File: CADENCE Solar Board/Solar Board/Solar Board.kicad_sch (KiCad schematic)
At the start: 44 parts, among them J1 Conn_01x08, U1 INA230AIRGTT, U2 AD7414ARTZ-1REEL7, U3 OPT3001IDNPRQ1

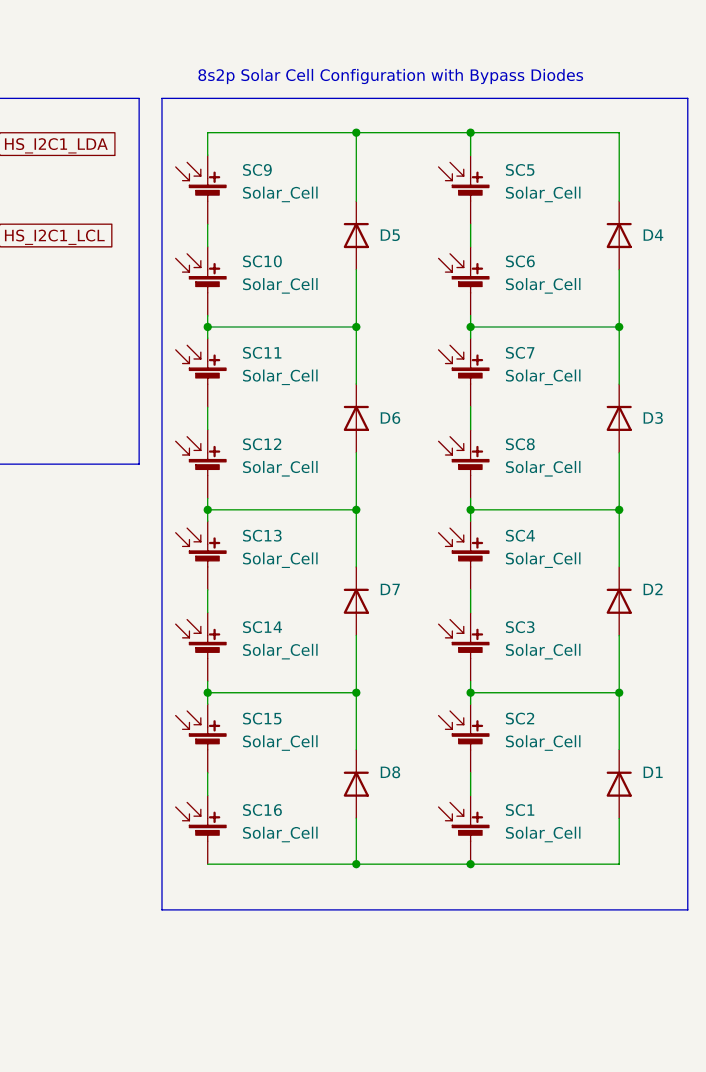
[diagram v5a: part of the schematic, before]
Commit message: fixed diodes
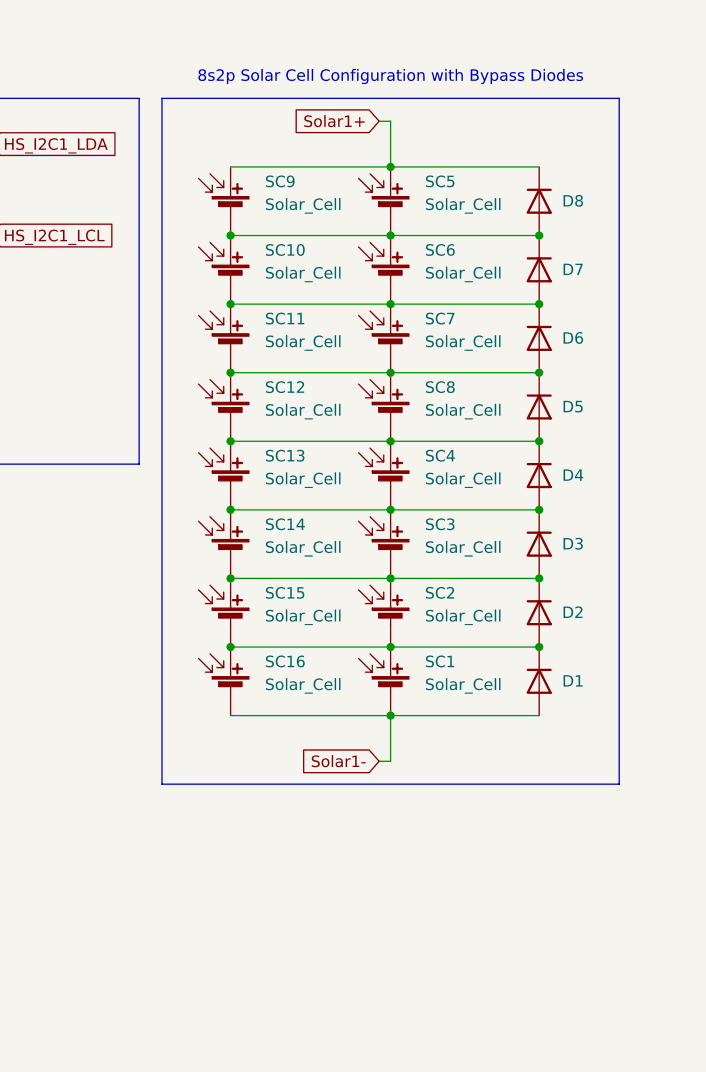
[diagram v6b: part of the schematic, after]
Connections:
- net Solar1+: now also D8.1 (K), SC5.1 (+), SC9.1 (+)
- net Solar1-: now also D1.2 (A), SC1.2 (-), SC16.2 (-)
- net at SC10.1 (+), SC9.2 (-): now also D7.1 (K), D8.2 (A), SC5.2 (-), SC6.1 (+)
- net at D6.1 (K), SC10.2 (-), SC11.1 (+): now also D7.2 (A), SC6.2 (-), SC7.1 (+); no longer D5.2 (A)
- net at SC11.2 (-), SC12.1 (+): now also D5.1 (K), D6.2 (A), SC7.2 (-), SC8.1 (+)
- net at SC12.2 (-), SC13.1 (+): now also D4.1 (K), D5.2 (A), SC4.1 (+), SC8.2 (-); no longer D6.2 (A), D7.1 (K)
- net at SC14.2 (-), SC15.1 (+): now also D2.1 (K), D3.2 (A), SC2.1 (+), SC3.2 (-); no longer D7.2 (A), D8.1 (K)
- net at D3.1 (K), D4.2 (A): now also SC13.2 (-), SC14.1 (+), SC3.1 (+), SC4.2 (-); no longer SC6.2 (-), SC7.1 (+)
- net at SC15.2 (-), SC16.1 (+): now also D1.1 (K), D2.2 (A), SC1.1 (+), SC2.2 (-)
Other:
- moved on the sheet: SC1, SC10, SC11, SC12, SC13, SC14, SC15, SC16, SC2, SC3, SC4, SC5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

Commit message: minor pcb and schematic updates
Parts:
- removed D1, D2, D3, D4, D5, D6, D7, D8: D, SK44BL-TP:DIOM4336X265N, symbol Device:D
- removed SC1, SC10, SC11, SC12, SC13, SC14, SC15, SC16, SC2, SC3, SC4, SC5, SC6, SC7, SC8, SC9: Solar_Cell, symbol Device:Solar_Cell
- D1: renamed from D19; footprint (none) -> LED_SMD:LED_RGB_Lumex_SML-LXT0805SIUGUBW
- D2: renamed from D20; footprint (none) -> LED_SMD:LED_RGB_Lumex_SML-LXT0805SIUGUBW
- R1, R2, R3, R4, R6, R7, R8: footprint Resistor_SMD:R_01005_0402Metric -> Resistor_SMD:R_0805_2012Metric
- R5: footprint (none) -> Resistor_SMD:R_0805_2012Metric
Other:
- note removed: "8s2p Solar Cell Configuration with Bypass Diodes"

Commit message: PCB Optimized (made smaller)
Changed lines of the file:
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@@
 		(property "Footprint" "Resistor_SMD:R_0805_2012Metric"
 			(at 39.624 41.656 90)
+			(hide yes)
 			(show_name no)
 			(do_not_autoplace no)
